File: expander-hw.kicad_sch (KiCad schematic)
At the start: 5 parts, among them J1 Conn_ARM_JTAG_SWD_10, J2 USB_C_Receptacle_USB2.0_16P, U1 STM32H562RGTx, U2 ECMF02-2AMX6, U3 AZ1117-3.3

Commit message: save
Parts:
- removed U2: ECMF02-2AMX6, Package_DFN_QFN:ST_UQFN-6L_1.5x1.7mm_P0.5mm, symbol Power_Protection:ECMF02-2AMX6
- added J3: Conn_02x08_Odd_Even, Connector_PinHeader_2.54mm:PinHeader_2x08_P2.54mm_Horizontal, symbol Connector_Generic:Conn_02x08_Odd_Even
- added R1, R2, R3, R4, R5, R6: 5k1, Resistor_SMD:R_0805_2012Metric, symbol Device:R
- added U2, U4, U6: SRDA3.3-4BTG, Package_SO:SOIC-8_3.9x4.9mm_P1.27mm, symbol expander-hw:TVS-Diode-Array4
- added U5: USBLC6-2SC6, Package_TO_SOT_SMD:SOT-23-6, symbol Power_Protection:USBLC6-2SC6
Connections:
- net +3.3V: now also J3.1 (Pin_1), R3.1, R4.1, R5.1, R6.1, U2.2 (VBUS), U2.3 (VBUS), U4.2 (VBUS), U4.3 (VBUS), U6.2 (VBUS), U6.3 (VBUS)
- net D+: now also U1.45 (PA12), U5.6 (I/O1)
- net D-: now also U1.44 (PA11), U5.4 (I/O2)
- net GND: now also R1.2, R2.2, U2.5 (GND), U2.8 (GND), U4.5 (GND), U4.8 (GND), U5.2 (GND), U6.5 (GND), U6.8 (GND)
- net VBUS: now also J3.2 (Pin_2), U5.5 (VBUS)
- net I2C2_SCL: now reaches U1.29 (PB10)
- net I2C2_SDA: now reaches U1.33 (PB12)
- net I2C3_SDA: now reaches U1.40 (PC9)
- net I2C3_SCL: now reaches U1.41 (PA8)
- net I2C1_SCL: now reaches U1.58 (PB6)
- net I2C1_SDA: now reaches U1.59 (PB7)
- net at J2.A6 (D+), J2.B6 (D+): now also U5.3 (I/O2)
- net at J2.A7 (D-), J2.B7 (D-): now also U5.1 (I/O1)
- net at J2.A5 (CC1): now also R1.1
- net at J2.B5 (CC2): now also R2.1
- new net: R6.2, U4.7 (I/O4)
- new net: R3.2, U4.1 (I/O1)
- new net: R4.2, U4.4 (I/O2)
- new net: R5.2, U4.6 (I/O3)

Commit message: save
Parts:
- added C1, C2, C3, C4: 100nF, Capacitor_SMD:C_0603_1608Metric, symbol Device:C
- added R7: 10k, Resistor_SMD:R_0603_1608Metric, symbol Device:R
- added X1: ECS-2520MV-xxx-xx, Crystal:Crystal_SMD_TXC_7M-4Pin_3.2x2.5mm, symbol Oscillator:ECS-2520MV-xxx-xx
- J3: footprint Connector_PinHeader_2.54mm:PinHeader_2x08_P2.54mm_Horizontal -> Connector_PinHeader_2.54mm:PinHeader_2x08_P2.54mm_Vertical
- R1, R2, R3, R4, R5, R6: footprint Resistor_SMD:R_0805_2012Metric -> Resistor_SMD:R_0603_1608Metric
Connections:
- net I2C2_SCL is gone; now on net SPI2_SCK: U1.29 (PB10)
- net +3.3V: now also C2.1, C3.1, C4.1, X1.1 (Tri-State), X1.4 (VDD)
- net D+: now also U5.3 (I/O2); no longer U5.6 (I/O1)
- net D-: now also U5.1 (I/O1); no longer U5.4 (I/O2)
- net GND: now also J3.11 (Pin_11), J3.12 (Pin_12), C1.2, C2.2, C3.2, C4.2, R7.1, X1.2 (GND)
- net I2C1_SCL: now also J3.16 (Pin_16), R3.2, U6.4 (I/O2)
- net I2C1_SDA: now also J3.15 (Pin_15), R4.2, U6.6 (I/O3)
- net I2C3_SCL: now also J3.14 (Pin_14), R5.2, U6.7 (I/O4)
- net I2C3_SDA: now also J3.13 (Pin_13), R6.2, U6.1 (I/O1)
- net ~{RESET}: now also U1.7 (NRST), C1.1
- net SPI1_MISO: now reaches U4.7 (I/O4)
- net SPI1_MISO: now also J3.4 (Pin_4), U1.22 (PA6); no longer R6.2
- net SPI1_SCK: now reaches U4.1 (I/O1)
- net SPI1_SCK: now also J3.3 (Pin_3), U1.21 (PA5); no longer R3.2
- net SPI1_CS: now reaches U4.4 (I/O2)
- net SPI1_CS: now also J3.6 (Pin_6), U1.14 (PA0); no longer R4.2
- net SPI1_MOSI: now reaches U4.6 (I/O3)
- net SPI1_MOSI: now also J3.5 (Pin_5), U1.23 (PA7); no longer R5.2
- net SPI2_SCK: now reaches U2.1 (I/O1)
- net SPI2_SCK: now also J3.7 (Pin_7)
- net SPI2_CS: now reaches U2.4 (I/O2)
- net SPI2_CS: now also J3.10 (Pin_10), U1.11 (PC3)
- net SPI2_MOSI: now reaches U2.6 (I/O3)
- net SPI2_MOSI: now also J3.9 (Pin_9), U1.9 (PC1)
- net SPI2_MISO: now reaches U2.7 (I/O4)
- net SPI2_MISO: now also J3.8 (Pin_8), U1.10 (PC2)
- net PH0: now reaches U1.5 (PH0)
- net PH0: now also X1.3 (OUT)
- net PH1: now reaches U1.6 (PH1)
- net at U1.60 (BOOT0): now also R7.2
- net at J2.A7 (D-), J2.B7 (D-): now also U5.4 (I/O2); no longer U5.1 (I/O1)
- net at J2.A6 (D+), J2.B6 (D+): now also U5.6 (I/O1); no longer U5.3 (I/O2)
- net I2C2_SDA: no longer names the net of U1.33 (PB12)
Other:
- moved on the sheet: J3, R1, R2, R3, R4, R5, R6, U2, U4, U5, U6

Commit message: Complete v1
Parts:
- added C5, C6, C7, C8: 10uF, Capacitor_SMD:C_0805_2012Metric, symbol Device:C
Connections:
- net +3.3V: now also C6.1, C7.1, C8.1
- net GND: now also C5.2, C6.2, C7.2, C8.2
- net VBUS: now also C5.1
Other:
- moved on the sheet: C2, C3, C4

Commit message: Add LED
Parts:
- added D1: LED, LED_SMD:LED_0603_1608Metric, symbol Device:LED
- added R8: 470, Resistor_SMD:R_0603_1608Metric, symbol Device:R
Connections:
- net GND: now also D1.1 (K)
- net LED_HRTB: now reaches U1.17 (PA3)
- net LED_HRTB: now also R8.1
- new net: D1.2 (A), R8.2
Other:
- moved on the sheet: C2, C3, C4, C5, C6, C7, C8, U3

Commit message: Fix vreg package
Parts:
- U3: footprint Package_TO_SOT_SMD:SOT-89-3 -> Package_TO_SOT_SMD:SOT-223-3_TabPin2
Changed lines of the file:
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@@
 	(label "LED_HRTB"
 		(at 87.63 134.62 0)
+		(fields_autoplaced yes)
 		(effects
 			(font
@@
 	(label "LED_HRTB"
 		(at 151.13 49.53 0)
+		(fields_autoplaced yes)
 		(effects
 			(font
@@
 			)
 		)
-		(property "Footprint" "Package_TO_SOT_SMD:SOT-89-3"
+		(property "Footprint" "Package_TO_SOT_SMD:SOT-223-3_TabPin2"
 			(at 36.83 138.43 0)
 			(effects

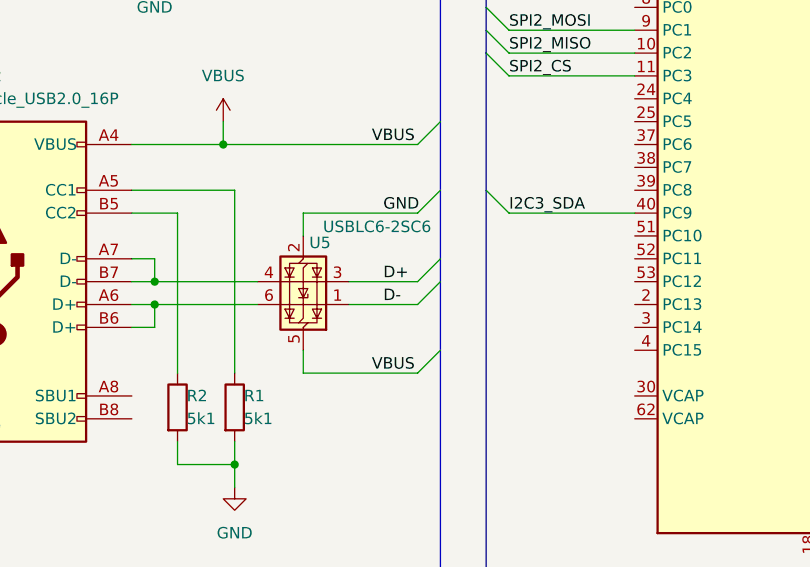
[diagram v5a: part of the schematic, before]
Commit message: Fix USB lines
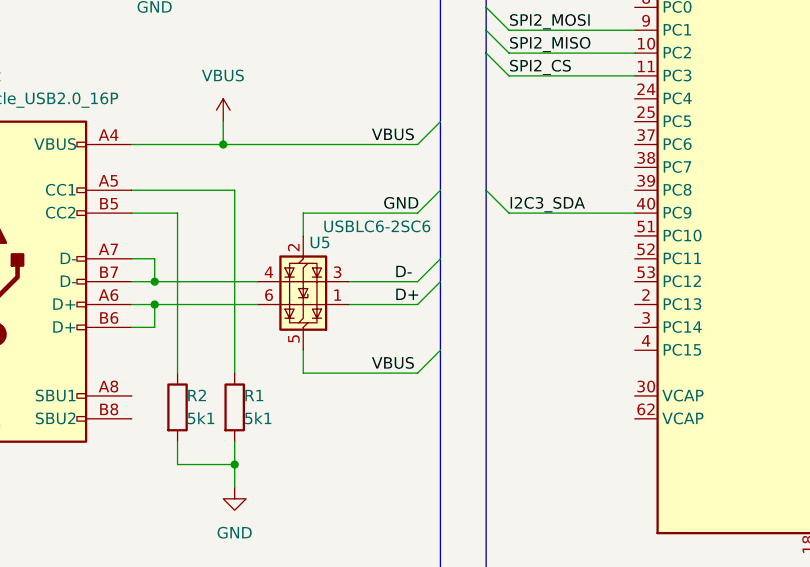
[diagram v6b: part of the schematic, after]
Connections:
- net D+: now also U5.1 (I/O1); no longer U5.3 (I/O2)
- net D-: now also U5.3 (I/O2); no longer U5.1 (I/O1)
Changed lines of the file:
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@@
 	)
 	(bus_entry
+		(at 80.01 92.71)
+		(size -2.54 2.54)
+		(stroke
+			(width 0)
+			(type default)
+		)
+	)
+	(bus_entry
 		(at 163.83 54.61)
 		(size -2.54 2.54)
@@
 	)
 	(bus_entry
-		(at 80.01 95.25)
+		(at 163.83 59.69)
 		(size -2.54 2.54)
 		(stroke
@@
 	)
 	(bus_entry
-		(at 163.83 59.69)
-		(size -2.54 2.54)
+		(at 85.09 39.37)
+		(size 2.54 2.54)
 		(stroke
 			(width 0)
@@
 	)
 	(bus_entry
-		(at 85.09 39.37)
-		(size 2.54 2.54)
+		(at 80.01 95.25)
+		(size -2.54 2.54)
 		(stroke
 			(width 0)
@@
 	)
 	(bus_entry
-		(at 80.01 92.71)
-		(size -2.54 2.54)
-		(stroke
-			(width 0)
-			(type default)
-		)
-	)
-	(bus_entry
 		(at 168.91 83.82)
 		(size 2.54 2.54)
@@
 	(wire
 		(pts
-			(xy 69.85 97.79) (xy 77.47 97.79)
-		)
-		(stroke
-			(width 0)
-			(type default)
-		)
-	)
-	(wire
-		(pts
 			(xy 87.63 41.91) (xy 101.6 41.91)
 		)
@@
 		)
 	)
+	(bus
+		(pts
+			(xy 80.01 95.25) (xy 80.01 102.87)
+		)
+		(stroke
+			(width 0)
+			(type default)
+		)
+	)
 	(wire
 		(pts
@@
 		)
 	)
+	(bus
+		(pts
+			(xy 80.01 92.71) (xy 80.01 95.25)
+		)
+		(stroke
+			(width 0)
+			(type default)
+		)
+	)
 	(wire
 		(pts
@@
 	(wire
 		(pts
+			(xy 69.85 97.79) (xy 77.47 97.79)
+		)
+		(stroke
+			(width 0)
+			(type default)
+		)
+	)
+	(wire
+		(pts
 			(xy 86.36 144.78) (xy 86.36 149.86)
 		)
@@
 	(wire
 		(pts
+			(xy 69.85 95.25) (xy 77.47 95.25)
+		)
+		(stroke
+			(width 0)
+			(type default)
+		)
+	)
+	(wire
+		(pts
 			(xy 101.6 144.78) (xy 101.6 148.59)
 		)
@@
 	(wire
 		(pts
-			(xy 69.85 95.25) (xy 77.47 95.25)
-		)
-		(stroke
-			(width 0)
-			(type default)
-		)
-	)
-	(wire
-		(pts
 			(xy 50.8 24.13) (xy 50.8 21.59)
 		)
@@
 		)
 	)
-	(bus
-		(pts
-			(xy 80.01 92.71) (xy 80.01 95.25)
-		)
-		(stroke
-			(width 0)
-			(type default)
-		)
-	)
 	(wire
 		(pts
@@
 	(bus
 		(pts
-			(xy 80.01 95.25) (xy 80.01 102.87)
-		)
-		(stroke
-			(width 0)
-			(type default)
-		)
-	)
-	(bus
-		(pts
 			(xy 163.83 52.07) (xy 163.83 54.61)
 		)
@@
 		)
 	)
-	(bus
-		(pts
-			(xy 80.01 85.09) (xy 80.01 92.71)
-		)
-		(stroke
-			(width 0)
-			(type default)
-		)
-	)
 	(wire
 		(pts
@@
 	(bus
 		(pts
+			(xy 80.01 85.09) (xy 80.01 92.71)
+		)
+		(stroke
+			(width 0)
+			(type default)
+		)
+	)
+	(bus
+		(pts
 			(xy 168.91 40.64) (xy 168.91 43.18)
 		)
@@
 		)
 	)
+	(label "D-"
+		(at 74.93 95.25 0)
+		(effects
+			(font
+				(size 1.27 1.27)
+			)
+			(justify left bottom)
+		)
+	)
 	(label "LED_HRTB"
 		(at 87.63 134.62 0)
@@
 		)
 	)
+	(label "D+"
+		(at 74.93 97.79 0)
+		(effects
+			(font
+				(size 1.27 1.27)
+			)
+			(justify left bottom)
+		)
+	)
 	(label "SPI2_MOSI"
 		(at 87.63 67.31 0)
@@
 		)
 	)
-	(label "D+"
-		(at 73.66 95.25 0)
-		(fields_autoplaced yes)
-		(effects
-			(font
-				(size 1.27 1.27)
-			)
-			(justify left bottom)
-		)
-	)
 	(label "SPI2_MISO"
 		(at 171.45 86.36 0)
@@
 		(fields_autoplaced yes)
 		(effects
-			(font
-				(size 1.27 1.27)
-			)
-			(justify left bottom)
-		)
-	)
-	(label "D-"
-		(at 73.66 97.79 0)
-		(fields_autoplaced yes)
-		(effects

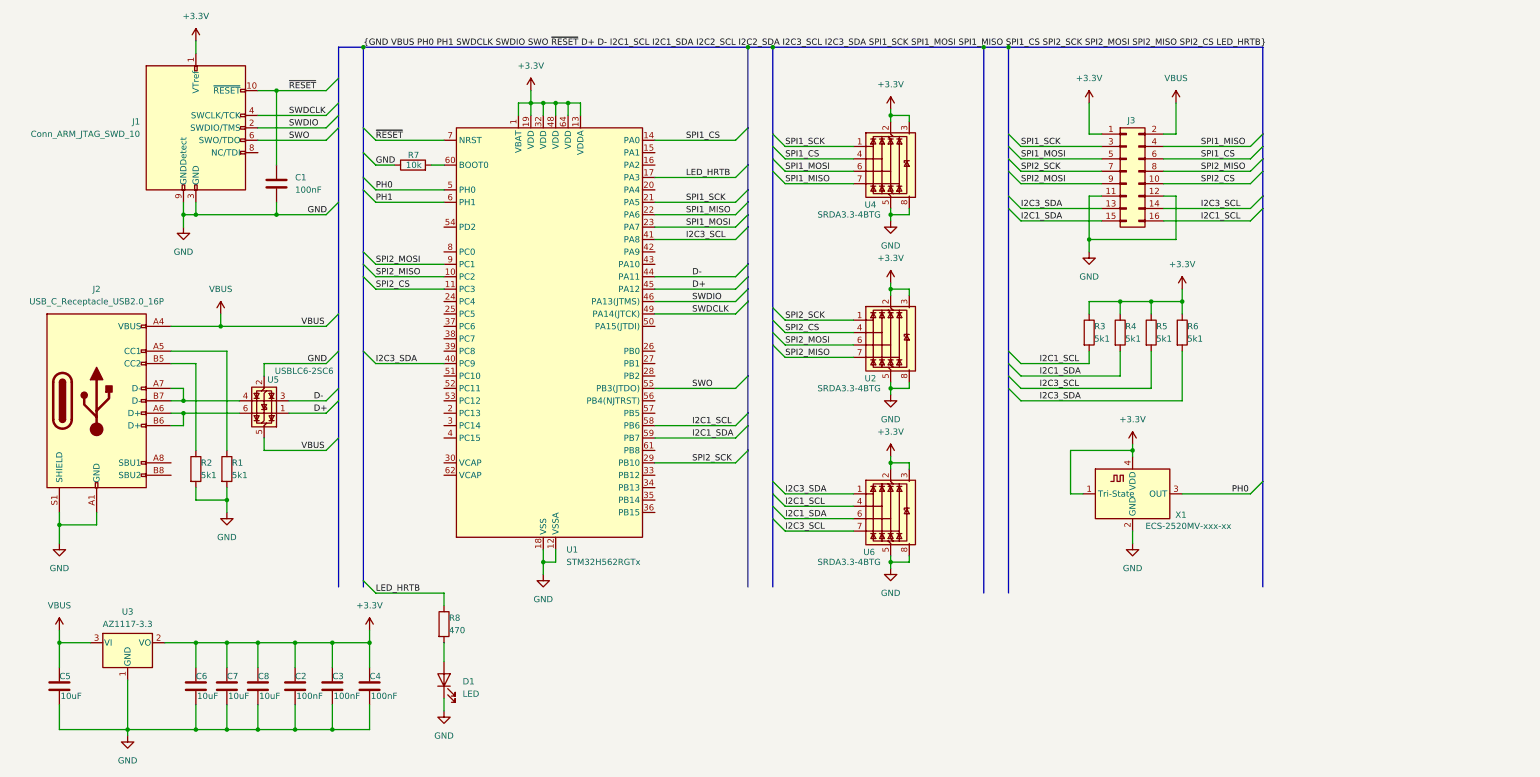
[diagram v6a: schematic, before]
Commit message: Move to STM32U545
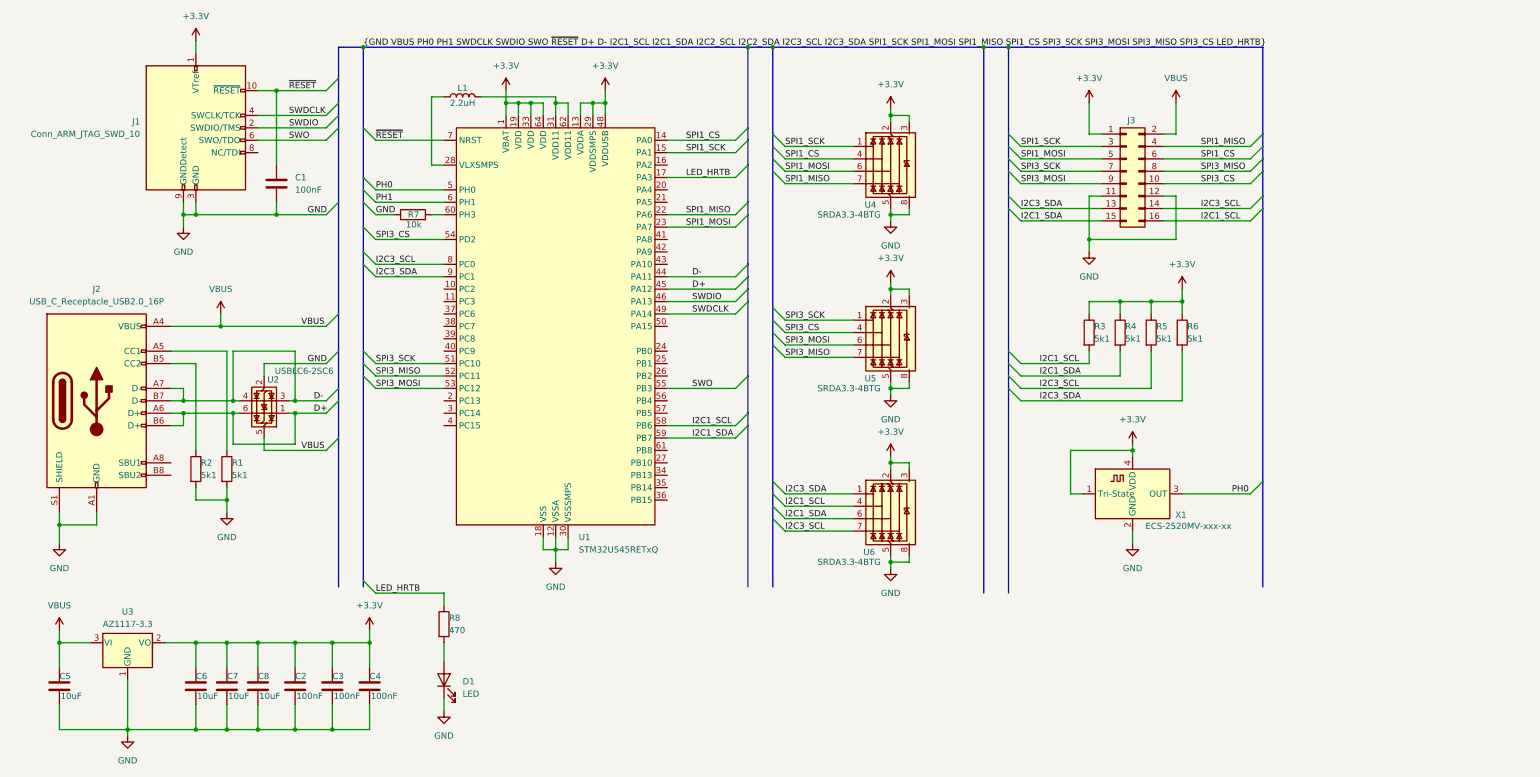
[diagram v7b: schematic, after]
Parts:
- removed U1: STM32H562RGTx, Package_QFP:LQFP-64_10x10mm_P0.5mm, symbol MCU_ST_STM32H5:STM32H562RGTx
- added L1: 2.2uH, Inductor_SMD:L_0805_2012Metric, symbol Device:L
- added U1: STM32U545RETxQ, Package_QFP:LQFP-64_10x10mm_P0.5mm, symbol MCU_ST_STM32U5:STM32U545RETxQ
- renumbered U5 to U2, U2 to U5
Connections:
- net +3.3V: now also U1.1 (VBAT), U1.13 (VDDA), U1.19 (VDD), U1.29 (VDDSMPS), U1.33 (VDD), U1.48 (VDDUSB), U1.64 (VDD)
- net D+: now also J2.A6 (D+), J2.B6 (D+), U2.6 (I/O1), U1.45 (PA12)
- net D-: now also J2.A7 (D-), J2.B7 (D-), U2.4 (I/O2), U1.44 (PA11)
- net GND: now also U1.12 (VSSA), U1.18 (VSS), U1.30 (VSSSMPS), U1.32 (VSS), U1.47 (VSS), U1.63 (VSS)
- net I2C1_SCL: now also U1.58 (PB6)
- net I2C1_SDA: now also U1.59 (PB7)
- net I2C3_SCL: now also U1.8 (PC0)
- net I2C3_SDA: now also U1.9 (PC1)
- net LED_HRTB: now also U1.17 (PA3)
- net PH0: now also U1.5 (PH0)
- net PH1: now also U1.6 (PH1)
- net SPI1_CS: now also U1.14 (PA0)
- net SPI1_MISO: now also U1.22 (PA6)
- net SPI1_MOSI: now also U1.23 (PA7)
- net SPI1_SCK: now also U1.15 (PA1)
- net SWDCLK: now also U1.49 (PA14)
- net SWDIO: now also U1.46 (PA13)
- net SWO: now also U1.55 (PB3)
- net ~{RESET}: now also U1.7 (NRST)
- net at R7.2: now also U1.60 (PH3)
- net SPI2_CS renamed SPI3_CS
- net SPI3_CS: now also U1.54 (PD2)
- net SPI2_MISO renamed SPI3_MISO
- net SPI3_MISO: now also U1.52 (PC11)
- net SPI2_MOSI renamed SPI3_MOSI
- net SPI3_MOSI: now also U1.53 (PC12)
- net SPI2_SCK renamed SPI3_SCK
- net SPI3_SCK: now also U1.51 (PC10)
- new net: L1.1, U1.28 (VLXSMPS)
- new net: L1.2, U1.31 (VDD11), U1.62 (VDD11)
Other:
- moved on the sheet: R7

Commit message: V2
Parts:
- added C9: 100nF, Capacitor_SMD:C_0603_1608Metric, symbol Device:C
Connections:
- net GND: now also C9.1
- net LED_HRTB: now also U1.42 (PA9); no longer U1.17 (PA3)
- net at L1.1, U1.28 (VLXSMPS): now also C9.2
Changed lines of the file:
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@@
 	)
 	(junction
+		(at 99.06 33.02)
+		(diameter 0)
+		(color 0 0 0 0)
+	)
+	(junction
 		(at 63.5 144.78)
 		(diameter 0)
@@
 	)
 	(bus_entry
+		(at 85.09 30.48)
+		(size 2.54 2.54)
+		(stroke
+			(width 0)
+			(type default)
+		)
+	)
+	(bus_entry
 		(at 217.17 53.34)
 		(size 2.54 2.54)
@@
 	)
 	(bus_entry
+		(at 163.83 62.23)
+		(size -2.54 2.54)
+		(stroke
+			(width 0)
+			(type default)
+		)
+	)
+	(bus_entry
 		(at 217.17 45.72)
 		(size 2.54 2.54)
@@
 	)
 	(bus_entry
-		(at 163.83 46.99)
-		(size -2.54 2.54)
-		(stroke
-			(width 0)
-			(type default)
-		)
-	)
-	(bus_entry
 		(at 168.91 114.3)
 		(size 2.54 2.54)
@@
 	(bus
 		(pts
+			(xy 85.09 30.48) (xy 85.09 39.37)
+		)
+		(stroke
+			(width 0)
+			(type default)
+		)
+	)
+	(bus
+		(pts
 			(xy 163.83 67.31) (xy 163.83 69.85)
 		)
@@
 	(wire
 		(pts
+			(xy 87.63 33.02) (xy 90.17 33.02)
+		)
+		(stroke
+			(width 0)
+			(type default)
+		)
+	)
+	(wire
+		(pts
 			(xy 64.77 87.63) (xy 64.77 90.17)
 		)
@@
 		)
 	)
+	(bus
+		(pts
+			(xy 163.83 62.23) (xy 163.83 67.31)
+		)
+		(stroke
+			(width 0)
+			(type default)
+		)
+	)
 	(wire
 		(pts
@@
 	(wire
 		(pts
+			(xy 97.79 33.02) (xy 99.06 33.02)
+		)
+		(stroke
+			(width 0)
+			(type default)
+		)
+	)
+	(wire
+		(pts
 			(xy 233.68 53.34) (xy 236.22 53.34)
 		)
@@
 	(bus
 		(pts
-			(xy 85.09 22.86) (xy 85.09 39.37)
-		)
-		(stroke
-			(width 0)
-			(type default)
-		)
-	)
-	(wire
-		(pts
-			(xy 147.32 49.53) (xy 161.29 49.53)
+			(xy 85.09 22.86) (xy 85.09 30.48)
 		)
 		(stroke
@@
 	(bus
 		(pts
-			(xy 163.83 41.91) (xy 163.83 46.99)
+			(xy 163.83 41.91) (xy 163.83 54.61)
 		)
 		(stroke
@@
 	(wire
 		(pts
+			(xy 147.32 64.77) (xy 161.29 64.77)
+		)
+		(stroke
+			(width 0)
+			(type default)
+		)
+	)
+	(wire
+		(pts
 			(xy 242.57 104.14) (xy 242.57 105.41)
 		)
@@
 		)
 	)
-	(bus
-		(pts
-			(xy 163.83 46.99) (xy 163.83 54.61)
-		)
-		(stroke
-			(width 0)
-			(type default)
-		)
-	)
 	(wire
 		(pts
@@
 	(bus
 		(pts
-			(xy 163.83 57.15) (xy 163.83 67.31)
+			(xy 163.83 57.15) (xy 163.83 62.23)
 		)
 		(stroke
@@
 	(label "SPI3_MISO"
 		(at 171.45 86.36 0)
+		(fields_autoplaced yes)
 		(effects
 			(font
@@
 	(label "SPI3_CS"
 		(at 171.45 81.28 0)
+		(fields_autoplaced yes)
 		(effects
 			(font
@@
 	)
 	(label "LED_HRTB"
-		(at 151.13 49.53 0)
-		(fields_autoplaced yes)
+		(at 151.13 64.77 0)
 		(effects
 			(font
@@
 	(label "SPI3_SCK"
 		(at 219.71 48.26 0)
+		(fields_autoplaced yes)
 		(effects
 			(font
@@
 	(label "SPI3_SCK"
 		(at 171.45 78.74 0)
+		(fields_autoplaced yes)
 		(effects
 			(font
@@
 	(label "SPI3_MISO"
 		(at 256.54 48.26 0)
+		(fields_autoplaced yes)
 		(effects
 			(font
@@
 	(label "SPI3_MOSI"
 		(at 219.71 50.8 0)
+		(fields_autoplaced yes)
 		(effects
 			(font
@@
 	(label "SPI3_CS"
 		(at 87.63 62.23 0)
+		(fields_autoplaced yes)
 		(effects
 			(font
@@
 		)
 	)
+	(label "GND"
+		(at 87.63 33.02 0)
+		(effects
+			(font
+				(size 1.27 1.27)
+			)
+			(justify left bottom)
+		)
+	)
 	(label "I2C3_SCL"
 		(at 223.52 92.71 0)
@@
 	(label "SPI3_CS"
 		(at 256.54 50.8 0)
+		(fields_autoplaced yes)
 		(effects
 			(font
@@
 	(label "SPI3_MOSI"
 		(at 171.45 83.82 0)
+		(fields_autoplaced yes)
 		(effects
 			(font
@@
 					(unit 1)
 				)
+			)
+		)
+	)
+	(symbol
+		(lib_id "Device:C")
+		(at 93.98 33.02 90)
+		(unit 1)
+		(exclude_from_sim no)
+		(in_bom yes)
+		(on_board yes)
+		(dnp no)
+		(property "Reference" "C9"
+			(at 93.98 29.718 90)
+			(effects
+				(font
+					(size 1.27 1.27)
+				)
+			)
+		)
+		(property "Value" "100nF"
+			(at 93.98 36.322 90)
+			(effects
+				(font
+					(size 1.27 1.27)
+				)
+			)
+		)
+		(property "Footprint" "Capacitor_SMD:C_0603_1608Metric"
+			(at 97.79 32.0548 0)
+			(effects
+				(font
+					(size 1.27 1.27)
+				)
+				(hide yes)
+			)
+		)
+		(property "Datasheet" "~"
+			(at 93.98 33.02 0)
+			(effects
+				(font
+					(size 1.27 1.27)
+				)
+				(hide yes)
+			)
+		)
+		(property "Description" "Unpolarized capacitor"
+			(at 93.98 33.02 0)
+			(effects
+				(font
+					(size 1.27 1.27)
+				)
+				(hide yes)
+			)
+		)
+		(pin "1"
+		)
+		(pin "2"
+		)
+		(instances
+			(project "expander-hw"
+				(path "/a3663717-3320-48fd-b38c-5475886dd95b"
+					(reference "C9")
+					(unit 1)
+				)
